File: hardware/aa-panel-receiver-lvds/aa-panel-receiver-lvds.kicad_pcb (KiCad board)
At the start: 2 copper layers, 67.3 x 50.8 mm, 44 parts, among them CN1 Conn_01x04, CN2 8P8C, CN3 Conn_01x02, J1 Conn_01x08, U1 MC3486N, U2 Si8640EB-B-IU, U3 LM4562, U4 CRE1S0505S3C

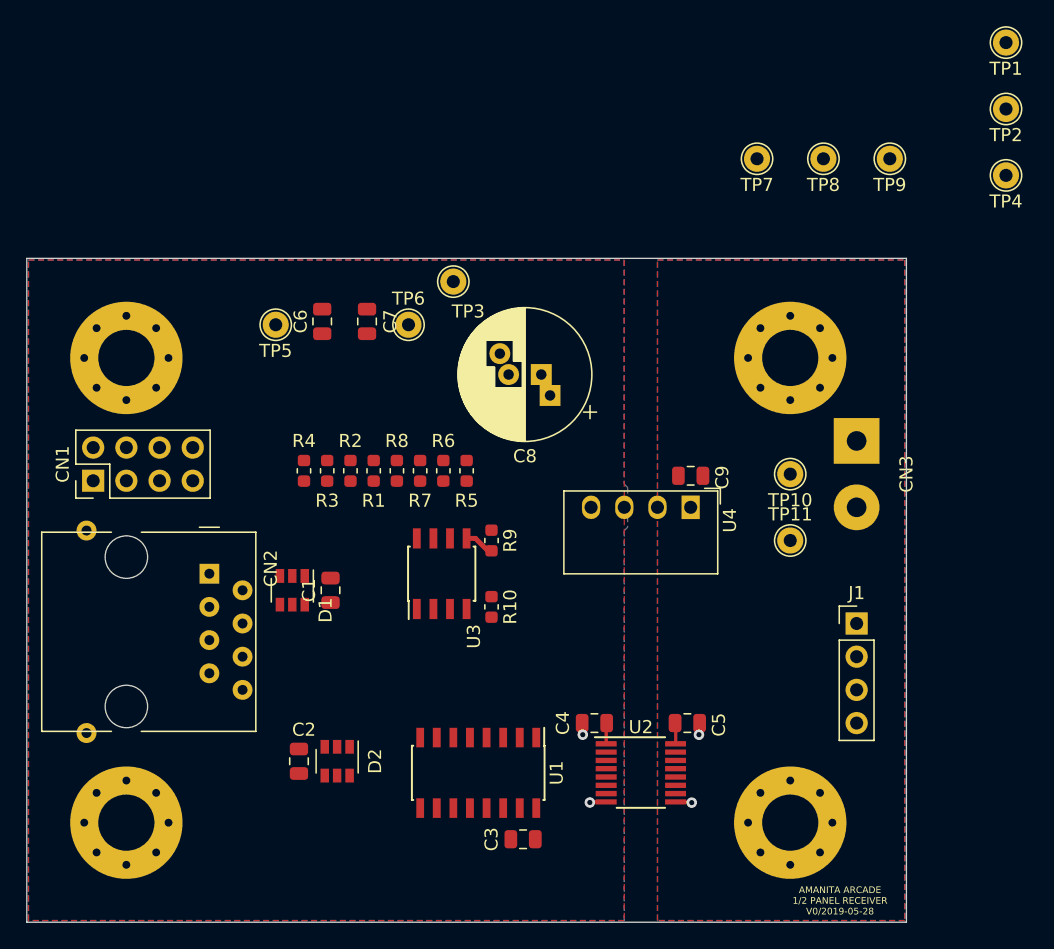
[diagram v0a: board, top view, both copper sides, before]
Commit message: Add power distro board, resolve some todos, finish a coherent layout of the panel receiver
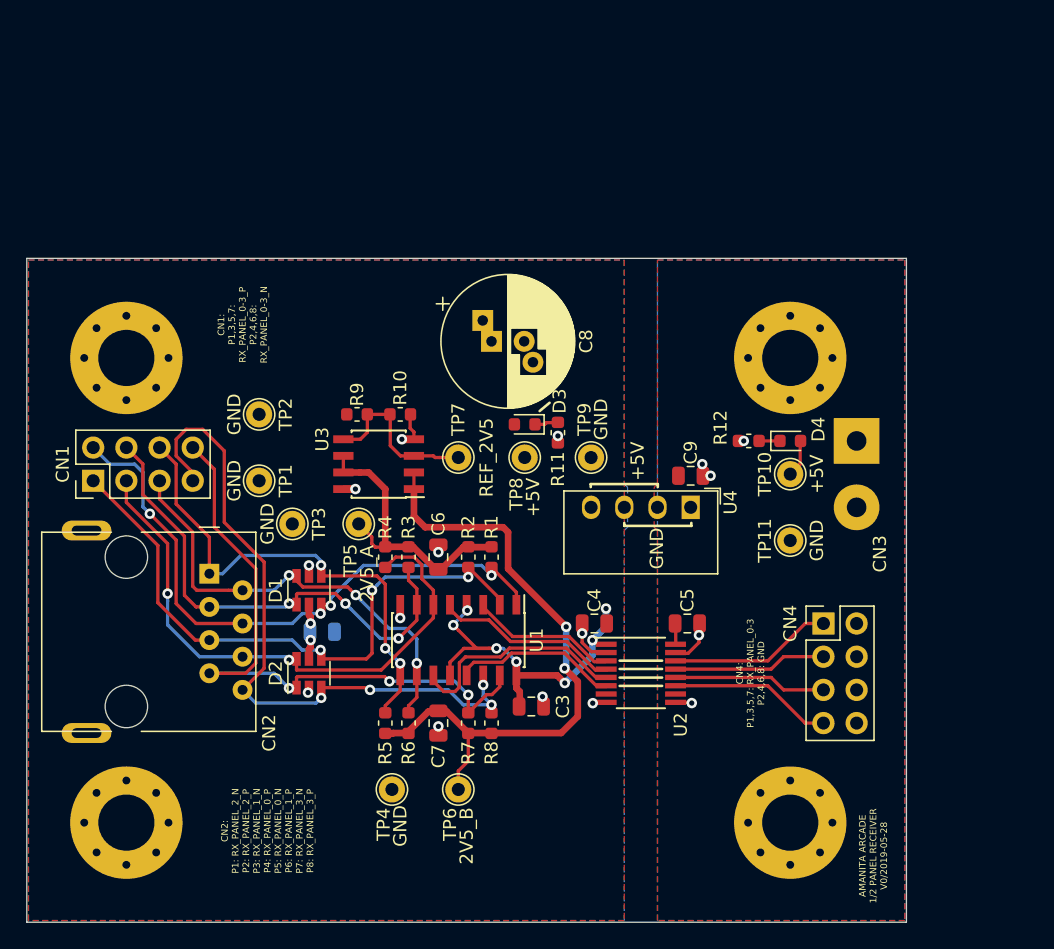
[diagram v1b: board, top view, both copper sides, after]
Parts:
- removed C2: 1u, Capacitor_SMD:C_0805_2012Metric
- removed J1: Conn_01x08, Connector_PinHeader_2.54mm:PinHeader_1x04_P2.54mm_Vertical
- added CN4: Conn_01x08, Connector_PinHeader_2.54mm:PinHeader_2x04_P2.54mm_Vertical, F.Cu at (152.4, 81.3)
- added D3: LED, Diode_SMD:D_0603_1608Metric, F.Cu at (129.5, 66.0)
- added D4: LED, Diode_SMD:D_0603_1608Metric, F.Cu at (149.9, 67.3)
- added R11: 470, Resistor_SMD:R_0603_1608Metric, F.Cu at (132.1, 66.7)
- added R12: 470, Resistor_SMD:R_0603_1608Metric, F.Cu at (146.7, 67.3)
- C1: moved to B.Cu
- moved TP4 66.5 mm to (119.4, 94.0), turned to 270 degrees
- moved TP1 66.3 mm to (109.2, 70.4), turned to 90 degrees
- moved TP2 61.7 mm to (109.2, 65.3), turned to 90 degrees
- moved TP6 35.8 mm to (124.5, 94.0), turned to 270 degrees
- moved TP8 32.3 mm to (129.5, 68.6), turned to 90 degrees
- moved TP7 32.3 mm to (124.5, 68.6), turned to 90 degrees
- moved TP9 32.3 mm to (134.6, 68.6), turned to 90 degrees
- moved C7 31.2 mm to (122.9, 88.9), turned to 270 degrees
- moved TP3 22.3 mm to (111.8, 73.7), turned to 270 degrees
- moved R8 20.6 mm to (127.0, 88.9), turned to 270 degrees
- moved R5 20.3 mm to (118.9, 88.9), turned to 270 degrees
- moved C6 20.1 mm to (122.9, 76.2)
- moved R7 19.7 mm to (125.2, 88.9), turned to 270 degrees
- moved R6 19.5 mm to (120.7, 88.9), turned to 270 degrees
- moved TP5 16.5 mm to (116.8, 73.7), turned to 270 degrees
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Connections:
- net GND_XY renamed GND
- net Net-(U1-Pad11) renamed /IN_TX_PANEL_2
- net Net-(U1-Pad13) renamed /IN_TX_PANEL_3
- net Net-(U1-Pad3) renamed /IN_TX_PANEL_0
- net Net-(U1-Pad5) renamed /IN_TX_PANEL_1
- D1 pad 1: /IN_TX_PANEL_0_P -> /IN_TX_PANEL_2_N
- D1 pad 3: /IN_TX_PANEL_0_N -> /IN_TX_PANEL_2_P
- D1 pad 4: /IN_TX_PANEL_1_P -> /IN_TX_PANEL_1_N
- D1 pad 6: /IN_TX_PANEL_1_N -> /IN_TX_PANEL_0_N
- D2 pad 1: /IN_TX_PANEL_2_P -> /IN_TX_PANEL_3_N
- D2 pad 3: /IN_TX_PANEL_2_N -> /IN_TX_PANEL_3_P
- D2 pad 4: /IN_TX_PANEL_3_P -> /IN_TX_PANEL_0_P
- D2 pad 6: /IN_TX_PANEL_3_N -> /IN_TX_PANEL_1_P
- R1 pad 1: /IN_TX_PANEL_0_P -> /IN_TX_PANEL_0_N
- R2 pad 1: /IN_TX_PANEL_0_N -> /IN_TX_PANEL_0_P
- R3 pad 1: /IN_TX_PANEL_1_P -> /IN_TX_PANEL_1_N
- R4 pad 1: /IN_TX_PANEL_1_N -> /IN_TX_PANEL_1_P
- R5 pad 1: /IN_TX_PANEL_2_P -> /IN_TX_PANEL_2_N
- R6 pad 1: /IN_TX_PANEL_2_N -> /IN_TX_PANEL_2_P
- R7 pad 1: /IN_TX_PANEL_3_P -> /IN_TX_PANEL_3_N
- R8 pad 1: /IN_TX_PANEL_3_N -> /IN_TX_PANEL_3_P
- U1 pad 1: /IN_TX_PANEL_0_P -> /IN_TX_PANEL_0_N
- U1 pad 10: /IN_TX_PANEL_2_N -> /IN_TX_PANEL_2_P
- U1 pad 14: /IN_TX_PANEL_3_N -> /IN_TX_PANEL_3_P
- U1 pad 15: /IN_TX_PANEL_3_P -> /IN_TX_PANEL_3_N
- U1 pad 2: /IN_TX_PANEL_0_N -> /IN_TX_PANEL_0_P
- U1 pad 6: /IN_TX_PANEL_1_N -> /IN_TX_PANEL_1_P
- U1 pad 7: /IN_TX_PANEL_1_P -> /IN_TX_PANEL_1_N
- U1 pad 9: /IN_TX_PANEL_2_P -> /IN_TX_PANEL_2_N
- U2 pad 11: Net-(J1-Pad4) -> /TX_PANEL_3
- U2 pad 12: Net-(J1-Pad3) -> /TX_PANEL_2
- U2 pad 13: Net-(J1-Pad2) -> /TX_PANEL_1
- U2 pad 14: Net-(J1-Pad1) -> /TX_PANEL_0
- U3 pad 1: /+2.5A -> /+2.5B
- U3 pad 2: /+2.5A -> /+2.5B
- U3 pad 6: /+2.5B -> /+2.5A
- U3 pad 7: /+2.5B -> /+2.5A
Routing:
- net /IN_TX_PANEL_3_P: track 0.00 -> 52.6 mm, vias 0 -> 4
- net /IN_TX_PANEL_3_N: track 0.00 -> 49.7 mm, vias 0 -> 3
- net /+2.5B: track 0.00 -> 48.7 mm, vias 0 -> 2
- net /IN_TX_PANEL_0_N: track 0.00 -> 47.7 mm, vias 0 -> 4
- net /IN_TX_PANEL_0_P: track 0.00 -> 47.3 mm, vias 0 -> 3
- net /IN_TX_PANEL_1_P: track 0.00 -> 44.2 mm, vias 0 -> 2
- net /IN_TX_PANEL_1_N: track 0.00 -> 38.7 mm, vias 0 -> 3
- net /IN_TX_PANEL_2_N: track 0.00 -> 37.9 mm, vias 0 -> 3
- net /IN_TX_PANEL_2_P: track 0.00 -> 34.9 mm, vias 0 -> 3
- net +5V_SX: track 1.59 -> 34.0 mm, vias 0 -> 10
- net /+2.5A: track 0.00 -> 22.0 mm
- net /IN_TX_PANEL_2: track 0.00 -> 17.4 mm
- net /IN_TX_PANEL_1: track 0.00 -> 14.3 mm
- net /IN_TX_PANEL_3: track 0.00 -> 12.7 mm
- net /TX_PANEL_3: track 0.00 -> 12.5 mm
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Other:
- net class Default: clearance 0.254 -> 0.127
- rule trace_clearance: 0.254 -> 0.127
- board text added: "+5V"
- board text added: "0N"
- board text added: "0P"
- board text added: "1N"
- board text added: "1P"
- board text added: "2N"
- board text added: "2P"
- board text added: "2V5_A"
- board text added: "2V5_B"
- board text added: "3N"
- board text added: "3P"
- board text added: "CN1: P1,3,5,7: RX_PANEL_0-3_P P2,4,6,8: RX_PANEL_0-3_N"
- board text added: "CN2: P1: RX_PANEL_2_N P2: RX_PANEL_2_P P3: RX_PANEL_1_N P4: RX_PANEL_0_P P5: RX_PANEL_0_N P6: RX_PANEL_1_P P7: RX_PANEL_3_N P8: RX_PANEL_3_P"
- board text added: "CN4: P1,3,5,7: RX_PANEL_0-3 P2,4,6,8: GND"
- board text added: "GND"
- board text added: "REF_2V5"

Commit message: Update to use a shared schematic component/footprint library
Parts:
- CN2: footprint aa-panel-receiver-lvds:8P8C_Assmann_A-2014-2S-4 -> aa-shared:8P8C_Assmann_A-2014-2S-4
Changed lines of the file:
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@@
       (net 1 /+2.5B))
   )
-  (module aa-panel-receiver-lvds:8P8C_Assmann_A-2014-2S-4 (layer F.Cu)
+  (module aa-shared:8P8C_Assmann_A-2014-2S-4 (layer F.Cu)
     (at 105.41 77.47 270)
     (descr http://www.assmann-wsw.com/fileadmin/datasheets/ASS_7330_CO.pdf)

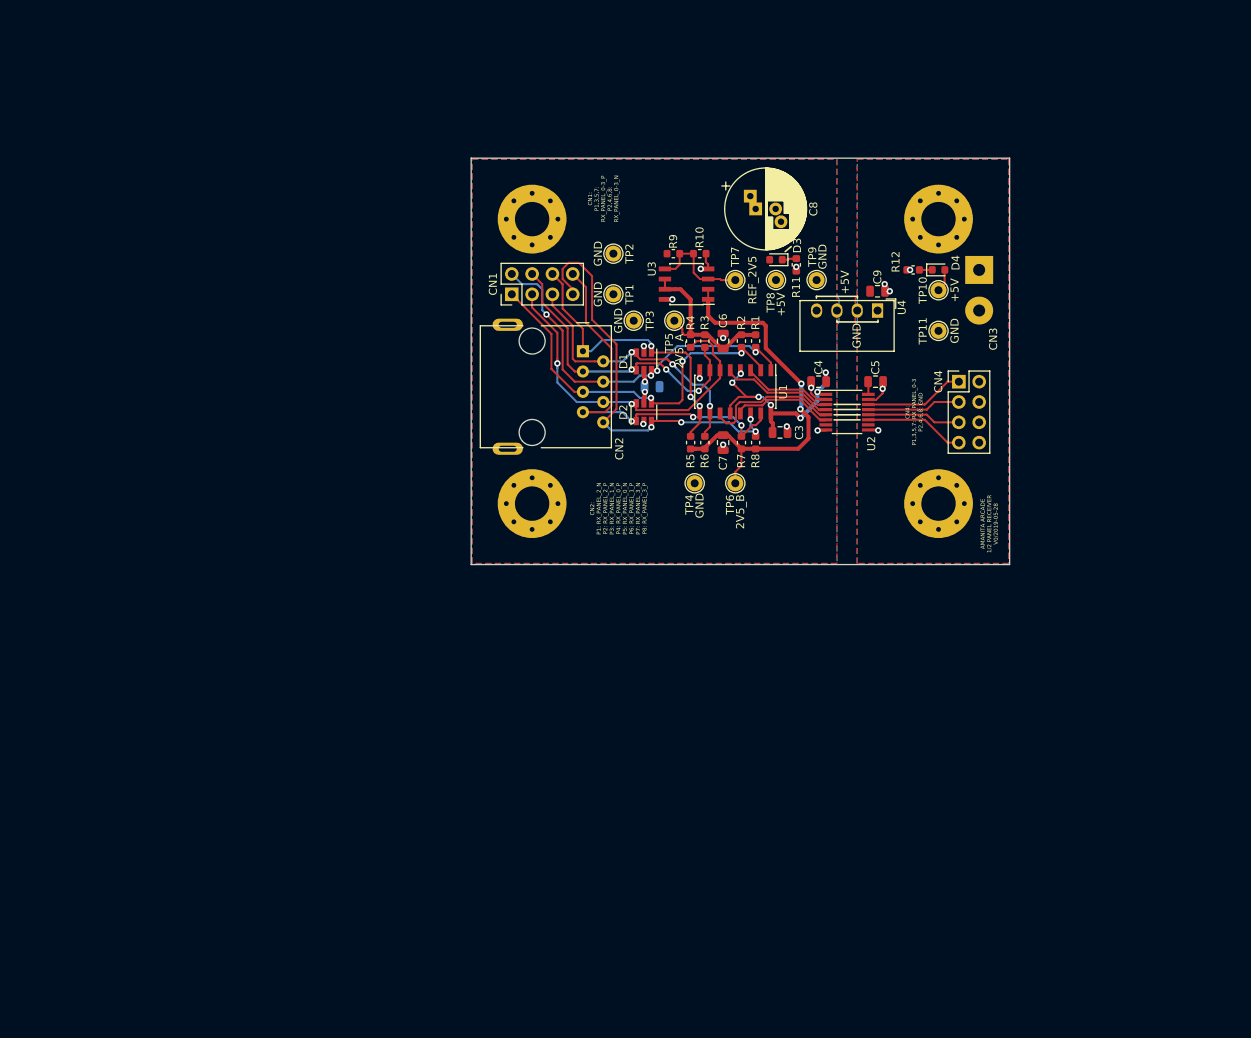
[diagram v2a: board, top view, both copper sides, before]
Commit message: Substantial rework of system, new layouts done for daughterboard, power, stalk receiver
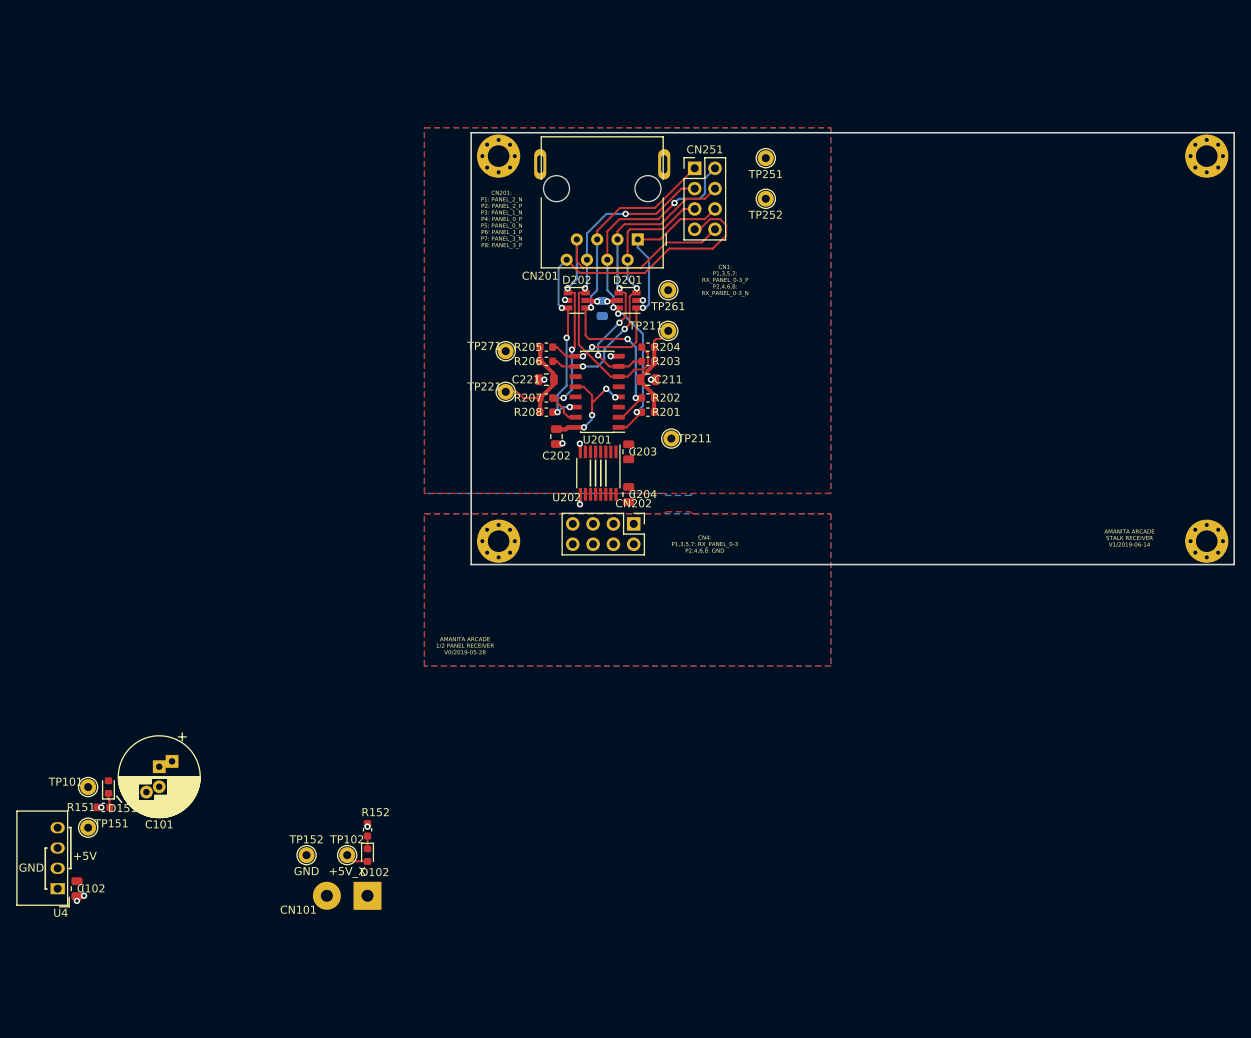
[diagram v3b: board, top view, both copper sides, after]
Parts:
- removed C3, C4, C5, C6, C7: 0.1u, Capacitor_SMD:C_0805_2012Metric
- removed C8: 100u, Capacitor_THT:CP_Radial_D10.0mm_P2.50mm_P5.00mm
- removed C9: 10u, Capacitor_SMD:C_0805_2012Metric
- removed CN1: Conn_01x04, Connector_PinHeader_2.54mm:PinHeader_2x04_P2.54mm_Vertical
- removed CN2: 8P8C, aa-shared:8P8C_Assmann_A-2014-2S-4
- removed CN3: Conn_01x02, Connector_Wire:SolderWirePad_1x02_P5.08mm_Drill1.5mm
- removed CN4: Conn_01x08, Connector_PinHeader_2.54mm:PinHeader_2x04_P2.54mm_Vertical
- removed D1, D2: D5V0P4UR6SO, Package_TO_SOT_SMD:SOT-23-6
- removed D3, D4: LED, Diode_SMD:D_0603_1608Metric
- removed R1, R2, R3, R4, R5, R6, R7, R8: 56, Resistor_SMD:R_0603_1608Metric
- removed R10, R9: 10k, Resistor_SMD:R_0603_1608Metric
- removed R11, R12: 470, Resistor_SMD:R_0603_1608Metric
- removed TP1, TP10, TP11, TP2, TP3, TP4, TP5, TP6, TP7, TP8, TP9: TestPoint, TestPoint:TestPoint_THTPad_D2.0mm_Drill1.0mm
- removed U1: MC3486N, Package_SO:SOIC-16_3.9x9.9mm_P1.27mm
- removed U2: Si8640EB-B-IU, Package_SO:QSOP-16_3.9x4.9mm_P0.635mm
- removed U3: LM4562, Package_SO:SOIC-8_3.9x4.9mm_P1.27mm
- added C101: 100u, Capacitor_THT:CP_Radial_D10.0mm_P2.50mm_P5.00mm, F.Cu at (52.5, 129.4)
- added C102: 10u, Capacitor_SMD:C_0805_2012Metric, F.Cu at (42.2, 144.7)
- added C202: 0.1u, Capacitor_SMD:C_0805_2012Metric, F.Cu at (102.1, 88.1)
- added C203: 0.1u, Capacitor_SMD:C_0805_2012Metric, F.Cu at (111.1, 90.0)
- added C204: 0.1u, Capacitor_SMD:C_0805_2012Metric, F.Cu at (111.1, 95.4)
- added C211: 0.1u, Capacitor_SMD:C_0805_2012Metric, F.Cu at (113.5, 81.0)
- added C221: 0.1u, Capacitor_SMD:C_0805_2012Metric, F.Cu at (100.8, 81.0)
- added CN101: Conn_01x02, Connector_Wire:SolderWirePad_1x02_P5.08mm_Drill1.5mm, F.Cu at (78.5, 145.5)
- added CN201: 8P8C, aa-shared:8P8C_Assmann_A-2014-2S-4, F.Cu at (112.3, 63.5)
- added CN202: Conn_01x08, Connector_PinHeader_2.54mm:PinHeader_2x04_P2.54mm_Vertical, F.Cu at (111.8, 99.1)
- added CN251: Conn_01x04, Connector_PinHeader_2.54mm:PinHeader_2x04_P2.54mm_Vertical, F.Cu at (119.4, 54.6)
- added D102: LED, Diode_SMD:D_0603_1608Metric, F.Cu at (78.5, 140.5)
- added D151: LED, Diode_SMD:D_0603_1608Metric, F.Cu at (46.1, 132.0)
- added D201: D5V0P4UR6SO, Package_TO_SOT_SMD:SOT-23-6, F.Cu at (111.0, 71.1)
- added D202: D5V0P4UR6SO, Package_TO_SOT_SMD:SOT-23-6, F.Cu at (104.6, 71.1)
- added R151: 470, Resistor_SMD:R_0603_1608Metric, F.Cu at (45.5, 134.5)
- added R152: 470, Resistor_SMD:R_0603_1608Metric, F.Cu at (78.5, 137.3)
- added R201: 56, Resistor_SMD:R_0603_1608Metric, F.Cu at (113.5, 85.1)
- added R202: 56, Resistor_SMD:R_0603_1608Metric, F.Cu at (113.5, 83.3)
- added R203: 56, Resistor_SMD:R_0603_1608Metric, F.Cu at (113.5, 78.7)
- added R204: 56, Resistor_SMD:R_0603_1608Metric, F.Cu at (113.5, 77.0)
- added R205: 56, Resistor_SMD:R_0603_1608Metric, F.Cu at (100.8, 77.0)
- added R206: 56, Resistor_SMD:R_0603_1608Metric, F.Cu at (100.8, 78.7)
- added R207: 56, Resistor_SMD:R_0603_1608Metric, F.Cu at (100.8, 83.3)
- added R208: 56, Resistor_SMD:R_0603_1608Metric, F.Cu at (100.8, 85.1)
- added TP101: TestPoint, TestPoint:TestPoint_THTPad_D2.0mm_Drill1.0mm, F.Cu at (43.6, 132.0)
- added TP102: TestPoint, TestPoint:TestPoint_THTPad_D2.0mm_Drill1.0mm, F.Cu at (75.9, 140.5)
- added TP151: TestPoint, TestPoint:TestPoint_THTPad_D2.0mm_Drill1.0mm, F.Cu at (43.6, 137.0)
- added TP152: TestPoint, TestPoint:TestPoint_THTPad_D2.0mm_Drill1.0mm, F.Cu at (70.9, 140.5)
- added TP211: TestPoint, TestPoint:TestPoint_THTPad_D2.0mm_Drill1.0mm, F.Cu at (116.1, 74.9)
- added TP211: TestPoint, TestPoint:TestPoint_THTPad_D2.0mm_Drill1.0mm, F.Cu at (116.5, 88.4)
- added TP221: TestPoint, TestPoint:TestPoint_THTPad_D2.0mm_Drill1.0mm, F.Cu at (95.8, 82.5)
- added TP251: TestPoint, TestPoint:TestPoint_THTPad_D2.0mm_Drill1.0mm, F.Cu at (128.3, 53.3)
- added TP252: TestPoint, TestPoint:TestPoint_THTPad_D2.0mm_Drill1.0mm, F.Cu at (128.3, 58.4)
- added TP261: TestPoint, TestPoint:TestPoint_THTPad_D2.0mm_Drill1.0mm, F.Cu at (116.1, 69.8)
- added TP271: TestPoint, TestPoint:TestPoint_THTPad_D2.0mm_Drill1.0mm, F.Cu at (95.8, 77.5)
- added U201: MC3486N, Package_SO:SOIC-16_3.9x9.9mm_P1.27mm, F.Cu at (107.2, 82.5)
- added U202: Si8640EB-B-IU, Package_SO:QSOP-16_3.9x4.9mm_P0.635mm, F.Cu at (107.3, 92.7)
- H1, H2, H3, H4: footprint MountingHole:MountingHole_4.3mm_M4_Pad_Via -> MountingHole:MountingHole_2.7mm_M2.5_Pad_Via
- moved U4 125.4 mm to (39.8, 144.7), turned to 180 degrees
- moved H2 94.9 mm to (183.4, 53.1)
- moved H3 68.2 mm to (94.9, 101.2)
- moved H4 33.9 mm to (183.4, 101.2)
- moved C1 11.6 mm to (107.8, 72.1), turned to 270 degrees
- moved H1 8.92 mm to (94.9, 53.1)
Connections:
- H2 pad 1: GND_S -> GND
- H3 pad 1: GND -> GND_S
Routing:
- net /+2.5B: track 48.7 -> 14.3 mm, vias 2 -> 0
- net /IN_TX_PANEL_2: track 17.4 -> 0.00 mm
- net /IN_TX_PANEL_1: track 14.3 -> 0.00 mm
- net Net-(R10-Pad1): track 13.2 -> 0.00 mm
- net /IN_TX_PANEL_3: track 12.7 -> 0.00 mm
- net /TX_PANEL_3: track 12.5 -> 0.00 mm
- net /TX_PANEL_0: track 12.5 -> 0.00 mm
- net +5V_SX: track 34.0 -> 21.9 mm, vias 10 -> 6
- net /TX_PANEL_2: track 11.7 -> 0.00 mm
- net /TX_PANEL_1: track 11.7 -> 0.00 mm
- net /IN_TX_PANEL_0: track 11.3 -> 0.00 mm
- net /+2.5A: track 22.0 -> 12.6 mm
- net GND_S: track 12.5 -> 5.84 mm, vias 10 -> 8
- net GND: track 6.76 -> 3.16 mm, vias 5 -> 4
- net +5V_X: track 4.43 -> 2.86 mm
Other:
- board size 67.3 x 50.8 mm -> 95.4 x 54 mm
- board text added: "+5V_X"
- board text added: "AMANITA ARCADE STALK RECEIVER V1/2019-06-14"
- board text added: "CN201: P1: PANEL_2_N P2: PANEL_2_P P3: PANEL_1_N P4: PANEL_0_P P5: PANEL_0_N P6: PANEL_1_P P7: PANEL_3_N P8: PANEL_3_P"
- board text removed: "2V5_A"
- board text removed: "2V5_B"
- board text removed: "CN2: P1: RX_PANEL_2_N P2: RX_PANEL_2_P P3: RX_PANEL_1_N P4: RX_PANEL_0_P P5: RX_PANEL_0_N P6: RX_PANEL_1_P P7: RX_PANEL_3_N P8: RX_PANEL_3_P"
- board text removed: "REF_2V5"
